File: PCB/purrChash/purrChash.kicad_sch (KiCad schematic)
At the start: 29 parts, among them J1 USB4135-GF-A_REVA, M1 Motor_DC_ALT, Q1 Q_NMOS_GSD, Q2 Q_PMOS_GSD, U1 MSP430FR2110/MSP430FR2111

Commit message: some layout work - will probably change
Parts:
- removed C6: 1u, Capacitor_SMD:C_0805_2012Metric, symbol pspice:CAP
- removed D4: D_Schottky, Diode_SMD:D_0603_1608Metric, symbol Device:D_Schottky
- removed Q2: Q_PMOS_GSD, Package_TO_SOT_SMD:SOT-23, symbol Device:Q_PMOS_GSD
- BT1: footprint Battery:BatteryHolder_Keystone_3034_1x20mm -> Connector_Wire:SolderWire-0.25sqmm_1x02_P4.2mm_D0.65mm_OD1.7mm
- D2: footprint LED_SMD:LED_0805_2012Metric -> LED_SMD:LED_2010_5025Metric_Pad1.52x2.65mm_HandSolder
- J1: footprint 6pos_usb:GCT_USB4135-GF-A_REVA -> Connector_USB:USB_C_Receptacle_GCT_USB4135-GF-A_6P_TopMnt_Horizontal
- M1: footprint (none) -> Connector_Wire:SolderWire-0.25sqmm_1x02_P4.2mm_D0.65mm_OD1.7mm
- U2: value (none) -> MCP73811T-420I-OT
- U3: value (none) -> TPS7A0533PDBZR
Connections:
- net VIN is gone; now on net VBAT: U3.1 (IN), U3.3 (EN)
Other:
- moved on the sheet: BT1, C4, C5, U2

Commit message: more pcb work
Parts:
- removed U2: MCP73811T-420I-OT, Package_TO_SOT_SMD:SOT-23-5, symbol Battery_Management:MCP73811T-420I-OT
- added D1: CHG_LED, LED_SMD:LED_0603_1608Metric, symbol Device:LED
- added D5: LED3, Library:LED_1206_3216Metric_shinethrough, symbol Device:LED
- added D6: LED4, Library:LED_1206_3216Metric_shinethrough, symbol Device:LED
- added R11, R12, R6: 1k, Resistor_SMD:R_0603_1608Metric, symbol Device:R
- added R3, R4, R5: 5.1k, Resistor_SMD:R_0603_1608Metric, symbol Device:R
- added U1: BQ21040DBV, Package_TO_SOT_SMD:SOT-23-6, symbol Battery_Management:BQ21040DBV
- D3: value LED -> LED1; footprint LED_SMD:LED_0805_2012Metric -> Library:LED_1206_3216Metric_shinethrough
- D4: renamed from D2; value LED -> LED2; footprint LED_SMD:LED_2010_5025Metric_Pad1.52x2.65mm_HandSolder -> Library:LED_1206_3216Metric_shinethrough
- TP1, TP2, TP3, TP4: footprint (none) -> Connector_Wire:SolderWirePad_1x01_SMD_1x2mm
- renumbered C4 to C1, C5 to C2, C7 to C3, C1 to C4, C2 to C5, C3 to C6, D1 to D2, R5 to R1, R2 to R10, R6 to R2, R1 to R7, R4 to R8, R3 to R9, U3 to U2, U1 to U3
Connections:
- net 3V3: now also D5.2 (A), D6.2 (A)
- net 5V_USB: now also U1.6 (VIN)
- net GND: now also R3.2, R5.2, U1.5 (GND)
- net LED1_R: now also D3.1 (K), R9.1; no longer D4.1 (K), R10.1
- net LED2_R: now also D4.1 (K), R10.1; no longer D3.1 (K), R9.1
- net VBAT: now also R6.1, U1.2 (OUT)
- net CHG: now reaches U3.4 (NRST/NMI/SBWTDIO)
- net CHG: now also D1.1 (K), U1.3 (~{CHG})
- net LED_MCU2: now reaches U3.9 (P2.1/TB0.2)
- net LED_MCU2: now also R11.2, R12.2
- net LED_MCU renamed LED_MCU1
- new net CHG_LED: D1.2 (A), R6.2
- new net ISET: R3.1, U1.4 (ISET)
- new net LED3_R: D5.1 (K), R11.1
- new net LED4_R: D6.1 (K), R12.1
- new net TS: R4.1, U1.1 (TS)
- new net TS_R: R4.2, R5.1
- no-connect marks 8 -> 6
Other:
- moved on the sheet: BT1, C1, C2, C4, D3, D4, R10, R9

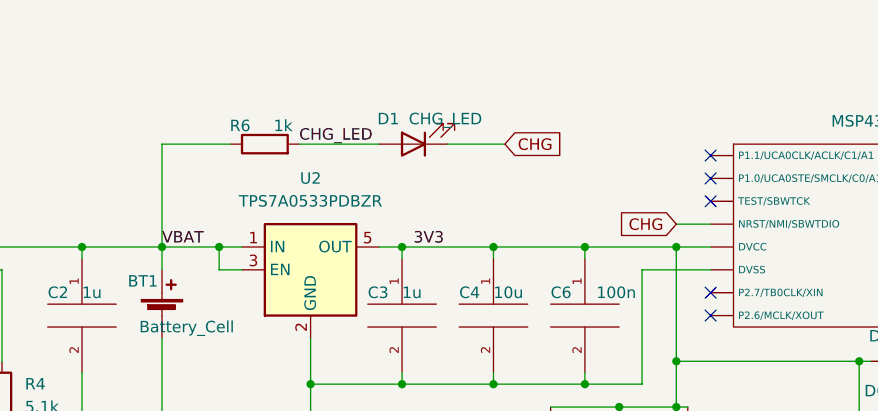
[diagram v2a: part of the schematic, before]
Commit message: pcb done with mouse-bite frame
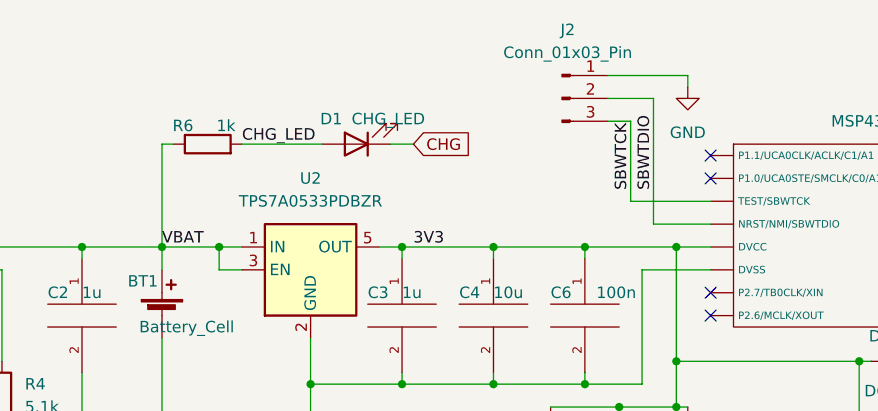
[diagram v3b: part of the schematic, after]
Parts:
- added J2: Conn_01x03_Pin, Connector_PinHeader_2.00mm:PinHeader_1x03_P2.00mm_Vertical, symbol Connector:Conn_01x03_Pin
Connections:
- net CHG: no longer U3.4 (NRST/NMI/SBWTDIO)
- net GND: now also J2.1 (Pin_1)
- net SBWTCK: now reaches U3.3 (TEST/SBWTCK)
- net SBWTCK: now also J2.3 (Pin_3)
- new net SBWTDIO: J2.2 (Pin_2), U3.4 (NRST/NMI/SBWTDIO)
- no-connect marks 6 -> 5
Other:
- moved on the sheet: D1, R6

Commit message: update BOM and fix some DNP and footprints
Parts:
- C6: footprint Capacitor_SMD:C_0603_1608Metric -> Capacitor_SMD:C_0402_1005Metric
- Q1: value Q_NMOS_GSD -> NXV55UNR
- U2: value TPS7A0533PDBZR -> TPS70933DBVR
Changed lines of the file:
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@@
 			)
 		)
-		(property "Description" ""
+		(property "Description" "CL21A106KAYNNNE"
 			(at 176.53 63.5 0)
 			(effects
@@
 			)
 		)
-		(property "Description" ""
+		(property "Description" "CL10A105KB8NNNC"
 			(at 76.2 54.61 0)
 			(effects
@@
 			)
 		)
-		(property "Value" "TPS7A0533PDBZR"
+		(property "Value" "TPS70933DBVR"
 			(at 149.86 34.29 0)
 			(effects
@@
 			)
 		)
-		(property "Datasheet" "https://www.ti.com/lit/ds/symlink/tps7a05.pdf"
+		(property "Datasheet" ""
 			(at 149.86 29.21 0)
 			(effects
@@
 			)
 		)
-		(property "Footprint" "Capacitor_SMD:C_0603_1608Metric"
+		(property "Footprint" "Capacitor_SMD:C_0402_1005Metric"
 			(at 180.34 46.99 0)
 			(effects
@@
 			)
 		)
-		(property "Description" ""
+		(property "Description" "CL05B104KO5NNNC"
 			(at 180.34 46.99 0)
 			(effects
@@
 			)
 		)
-		(property "Description" ""
+		(property "Description" "CL10A105KB8NNNC"
 			(at 160.02 46.99 0)
 			(effects
@@
 			)
 		)
-		(property "Description" ""
+		(property "Description" "CL21A106KAYNNNE"
 			(at 170.18 46.99 0)
 			(effects
@@
 			)
 		)
-		(property "Value" "Q_NMOS_GSD"
+		(property "Value" "NXV55UNR"
 			(at 187.96 92.71 90)
 			(effects
@@
 			)
 		)
-		(property "Description" ""
+		(property "Description" "SD0603S040S0R2"
 			(at 184.15 64.77 0)
 			(effects
@@
 			)
 		)
-		(property "Description" ""
+		(property "Description" "CL10A105KB8NNNC"
 			(at 124.46 46.99 0)
 			(effects

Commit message: many changes😅
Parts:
- C1, C2, C3: footprint Capacitor_SMD:C_0805_2012Metric -> Capacitor_SMD:C_0603_1608Metric
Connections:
- net GND: no longer C5.2, D2.2 (A)
- net MOTOR_GND: now also C5.2, D2.2 (A)
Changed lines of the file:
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@@
 	)
 	(junction
+		(at 191.77 69.85)
+		(diameter 0)
+		(color 0 0 0 0)
+	)
+	(junction
 		(at 124.46 93.98)
 		(diameter 0)
@@
 	)
 	(junction
-		(at 180.34 69.85)
-		(diameter 0)
-		(color 0 0 0 0)
-	)
-	(junction
-		(at 180.34 93.98)
-		(diameter 0)
-		(color 0 0 0 0)
-	)
-	(junction
 		(at 160.02 39.37)
 		(diameter 0)
@@
 	)
 	(junction
+		(at 184.15 69.85)
+		(diameter 0)
+		(color 0 0 0 0)
+	)
+	(junction
 		(at 76.2 93.98)
 		(diameter 0)
@@
 	(wire
 		(pts
-			(xy 149.86 93.98) (xy 180.34 93.98)
+			(xy 149.86 93.98) (xy 191.77 93.98)
 		)
 		(stroke
@@
 	(wire
 		(pts
-			(xy 180.34 69.85) (xy 180.34 93.98)
+			(xy 191.77 69.85) (xy 191.77 80.01)
 		)
 		(stroke
@@
 	(wire
 		(pts
+			(xy 176.53 69.85) (xy 184.15 69.85)
+		)
+		(stroke
+			(width 0)
+			(type default)
+		)
+	)
+	(wire
+		(pts
 			(xy 191.77 57.15) (xy 190.5 57.15)
 		)
@@
 	(wire
 		(pts
-			(xy 76.2 39.37) (xy 85.09 39.37)
+			(xy 184.15 69.85) (xy 191.77 69.85)
 		)
 		(stroke
@@
 	(wire
 		(pts
-			(xy 187.96 22.86) (xy 187.96 36.83)
+			(xy 76.2 39.37) (xy 85.09 39.37)
 		)
 		(stroke
@@
 	(wire
 		(pts
-			(xy 210.82 58.42) (xy 210.82 64.77)
+			(xy 187.96 22.86) (xy 187.96 36.83)
 		)
 		(stroke
@@
 	(wire
 		(pts
-			(xy 133.35 39.37) (xy 139.7 39.37)
+			(xy 210.82 58.42) (xy 210.82 64.77)
 		)
 		(stroke
@@
 	(wire
 		(pts
-			(xy 124.46 39.37) (xy 124.46 40.64)
+			(xy 133.35 39.37) (xy 139.7 39.37)
 		)
 		(stroke
@@
 	(wire
 		(pts
-			(xy 180.34 69.85) (xy 184.15 69.85)
+			(xy 124.46 39.37) (xy 124.46 40.64)
 		)
 		(stroke
@@
 	(wire
 		(pts
-			(xy 176.53 69.85) (xy 180.34 69.85)
-		)
-		(stroke
-			(width 0)
-			(type default)
-		)
-	)
-	(wire
-		(pts
 			(xy 190.5 39.37) (xy 194.31 39.37)
 		)
@@
 	(wire
 		(pts
-			(xy 180.34 93.98) (xy 191.77 93.98)
-		)
-		(stroke
-			(width 0)
-			(type default)
-		)
-	)
-	(wire
-		(pts
 			(xy 149.86 54.61) (xy 149.86 93.98)
 		)
@@
 	(wire
 		(pts
-			(xy 191.77 69.85) (xy 191.77 80.01)
-		)
-		(stroke
-			(width 0)
-			(type default)
-		)
-	)
-	(wire
-		(pts
 			(xy 149.86 49.53) (xy 149.86 54.61)
 		)
@@
 		)
 	)
+	(label "MOTOR_GND"
+		(at 191.77 72.39 180)
+		(fields_autoplaced yes)
+		(effects
+			(font
+				(size 1.27 1.27)
+			)
+			(justify right bottom)
+		)
+	)
 	(label "LED_MCU1"
 		(at 251.46 72.39 180)
@@
 		)
 	)
-	(label "MOTOR_GND"
-		(at 191.77 69.85 270)
-		(fields_autoplaced yes)
-		(effects
-			(font
-				(size 1.27 1.27)
-			)
-			(justify right bottom)
-		)
-	)
 	(label "LED2_R"
 		(at 228.6 72.39 180)
@@
 			)
 		)
-		(property "Footprint" "Capacitor_SMD:C_0805_2012Metric"
+		(property "Footprint" "Capacitor_SMD:C_0603_1608Metric"
 			(at 76.2 54.61 0)
 			(effects
@@
 			)
 		)
-		(property "Footprint" "Capacitor_SMD:C_0805_2012Metric"
+		(property "Footprint" "Capacitor_SMD:C_0603_1608Metric"
 			(at 160.02 46.99 0)
 			(effects
@@
 			)
 		)
-		(property "Footprint" "Capacitor_SMD:C_0805_2012Metric"
+		(property "Footprint" "Capacitor_SMD:C_0603_1608Metric"
 			(at 124.46 46.99 0)
 			(effects
